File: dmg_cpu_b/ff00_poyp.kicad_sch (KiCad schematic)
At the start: 67 parts, among them P10 IOBUF_B, P11 IOBUF_B, P12 IOBUF_B, P13 IOBUF_B, P14 OBUF_B, P15 OBUF_B

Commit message: First lot of fixes based on issues found.
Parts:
- removed ADYR, AFOP: INVERTER_B, symbol DMG_CPU_Cells:INVERTER_B
- removed AJEC, AKAJ, ANOC, ARAR, ASUZ, ATAJ, BEDA, BENU: TRI_INV_IF0, symbol DMG_CPU_Cells:TRI_INV_IF0
- removed APYS: NOR_2, symbol DMG_CPU_Cells:NOR_2
- removed AXYN: INVERTER_A, symbol DMG_CPU_Cells:INVERTER_A
- ACAT: value NAND_4 -> AND_4; symbol DMG_CPU_Cells:NAND_4 -> DMG_CPU_Cells:AND_4
- CUDY, JEKU, KEMA, KOCE, KURO, KUVE: value TRI_INV_IF1 -> TRI_INV_IF0; symbol DMG_CPU_Cells:TRI_INV_IF1 -> DMG_CPU_Cells:TRI_INV_IF0
- gave numbers to parts that had none: 2
- renumbered JEKU to KOLO
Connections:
- net FF60_D0: now also SIN.3 (~{ENA}_PU)
- net GND: no longer SIN.3 (~{ENA}_PU)
- net at AWOB.2 (D), BATU.3 (D), KERY.5: no longer ASOK.2
- net at ACEF.3 (D), BATU.6 (Q): now also ASOK.2
- net SIN renamed ~{SIN}
- net ~{FF00RD} renamed FF00RD
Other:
- note removed: "This part is in theory never activated."
- moved on the sheet: AKUG, AMUS, ANAP, ATOZ, BYKO

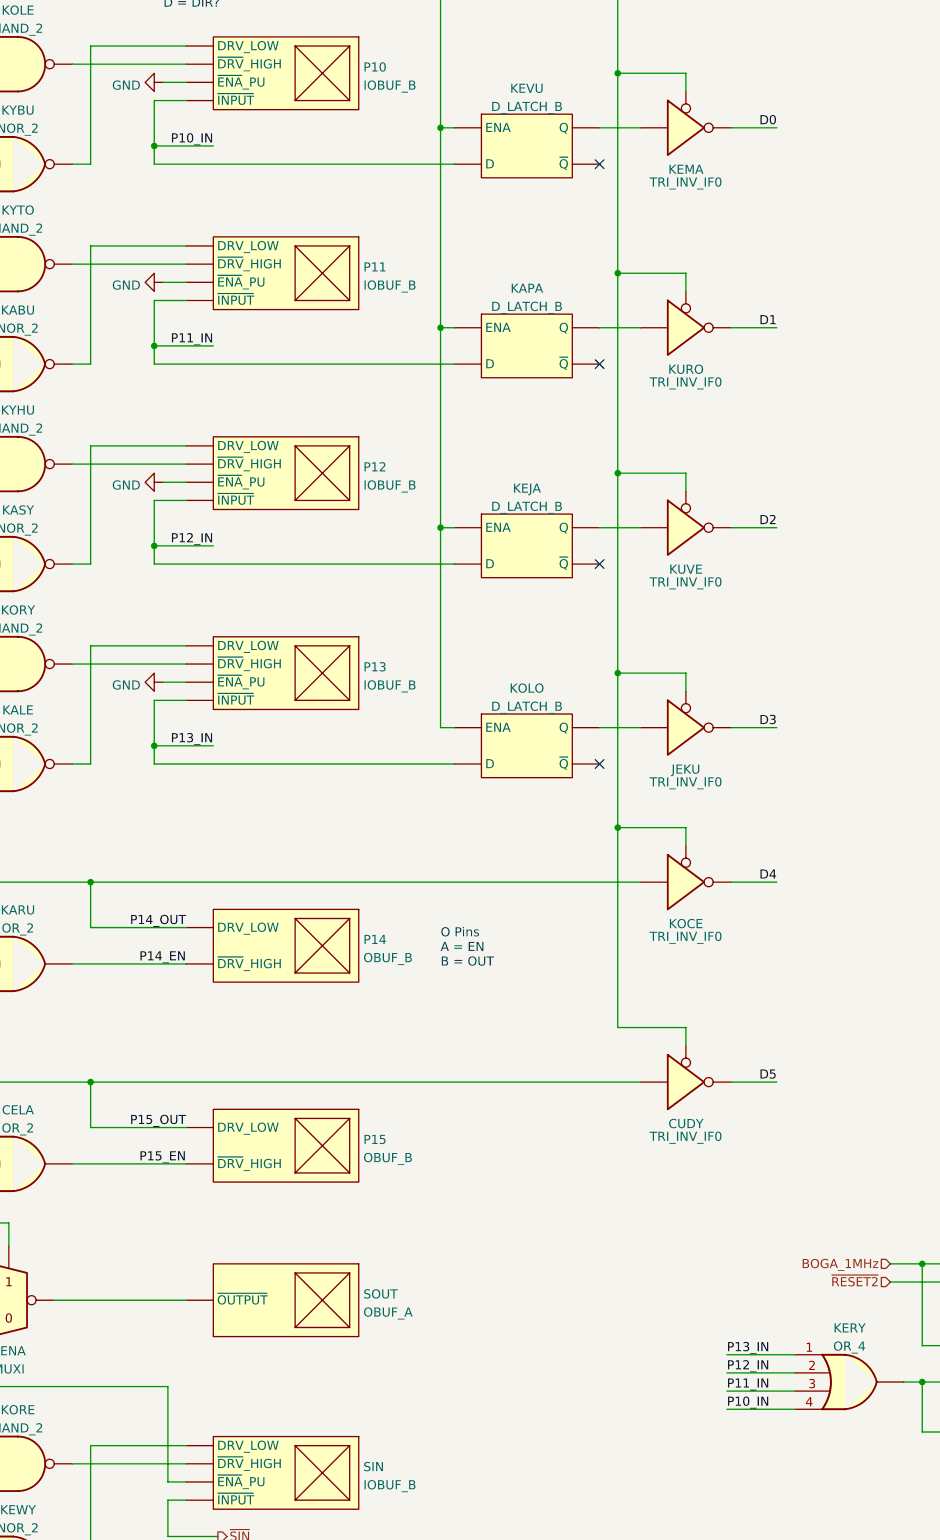
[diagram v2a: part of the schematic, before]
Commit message: CH1 SWEEP page added.
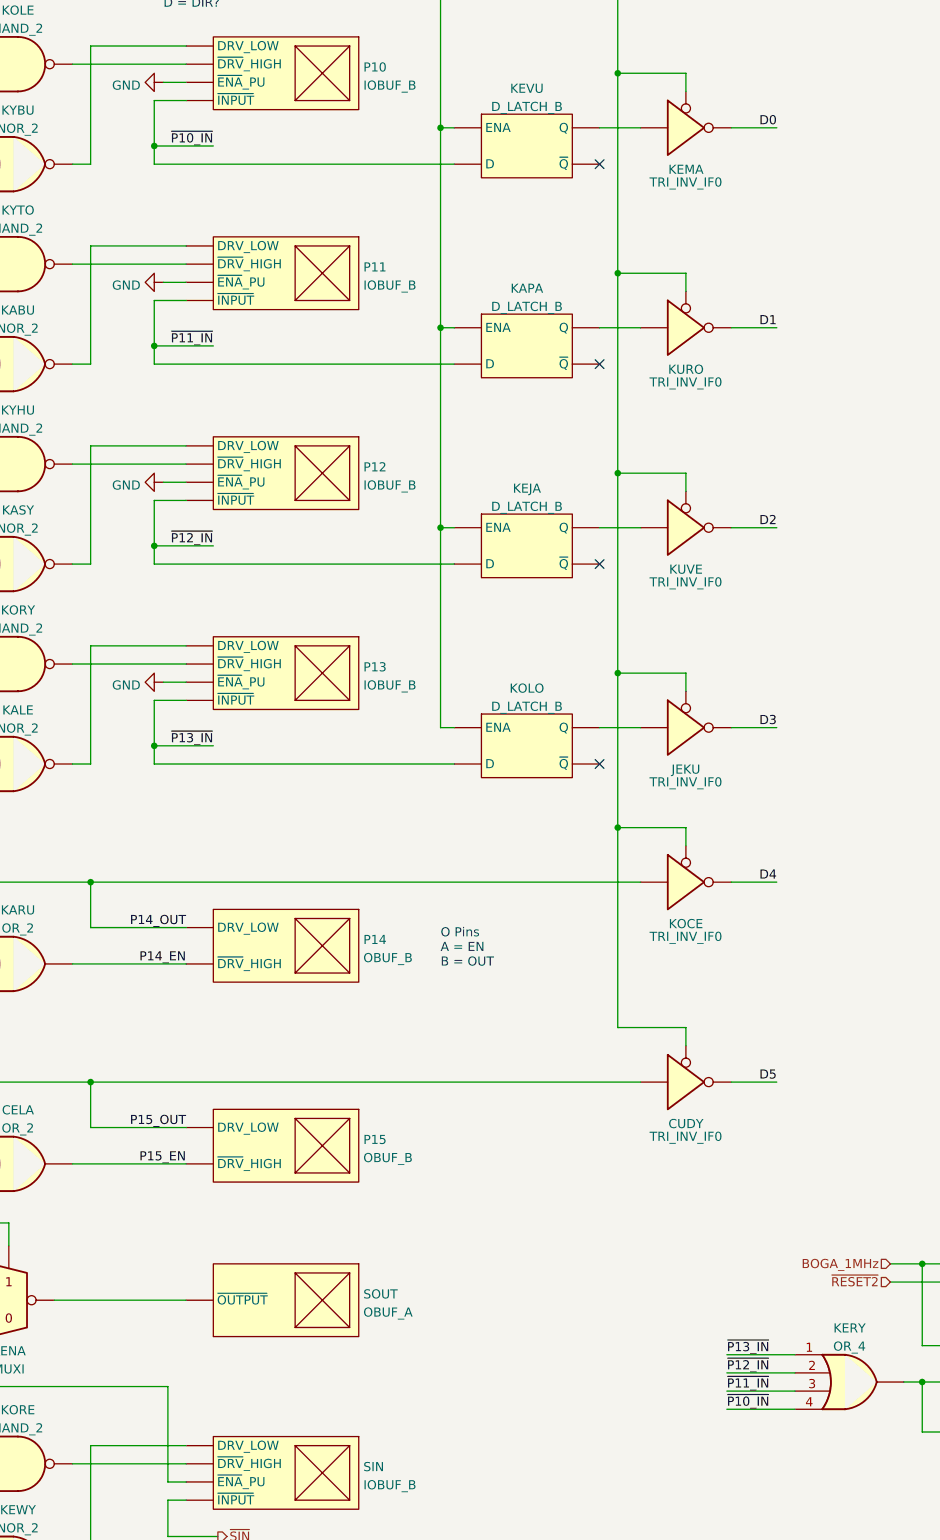
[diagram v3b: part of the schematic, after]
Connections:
- net P10_IN renamed ~{P10_IN}
- net P11_IN renamed ~{P11_IN}
- net P12_IN renamed ~{P12_IN}
- net P13_IN renamed ~{P13_IN}
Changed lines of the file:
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@@
     (effects (font (size 1.27 1.27)) (justify left bottom))
   )
-  (label "P13_IN" (at 184.15 226.695 0)
+  (label "~{P13_IN}" (at 184.15 226.695 0)
     (effects (font (size 1.27 1.27)) (justify left bottom))
   )
-  (label "P11_IN" (at 184.15 231.775 0)
+  (label "~{P11_IN}" (at 184.15 231.775 0)
     (effects (font (size 1.27 1.27)) (justify left bottom))
   )
@@
     (effects (font (size 1.27 1.27)) (justify right bottom))
   )
-  (label "P12_IN" (at 184.15 229.235 0)
+  (label "~{P12_IN}" (at 184.15 229.235 0)
     (effects (font (size 1.27 1.27)) (justify left bottom))
   )
-  (label "P11_IN" (at 112.395 85.725 180)
+  (label "~{P11_IN}" (at 112.395 85.725 180)
     (effects (font (size 1.27 1.27)) (justify right bottom))
   )
@@
     (effects (font (size 1.27 1.27)) (justify right bottom))
   )
-  (label "P13_IN" (at 112.395 141.605 180)
+  (label "~{P13_IN}" (at 112.395 141.605 180)
     (effects (font (size 1.27 1.27)) (justify right bottom))
   )
@@
     (effects (font (size 1.27 1.27)) (justify left bottom))
   )
-  (label "P10_IN" (at 184.15 234.315 0)
+  (label "~{P10_IN}" (at 184.15 234.315 0)
     (effects (font (size 1.27 1.27)) (justify left bottom))
   )
@@
     (effects (font (size 1.27 1.27)) (justify right bottom))
   )
-  (label "P10_IN" (at 112.395 57.785 180)
+  (label "~{P10_IN}" (at 112.395 57.785 180)
     (effects (font (size 1.27 1.27)) (justify right bottom))
   )
@@
     (effects (font (size 1.27 1.27)) (justify left bottom))
   )
-  (label "P12_IN" (at 112.395 113.665 180)
+  (label "~{P12_IN}" (at 112.395 113.665 180)
     (effects (font (size 1.27 1.27)) (justify right bottom))
   )

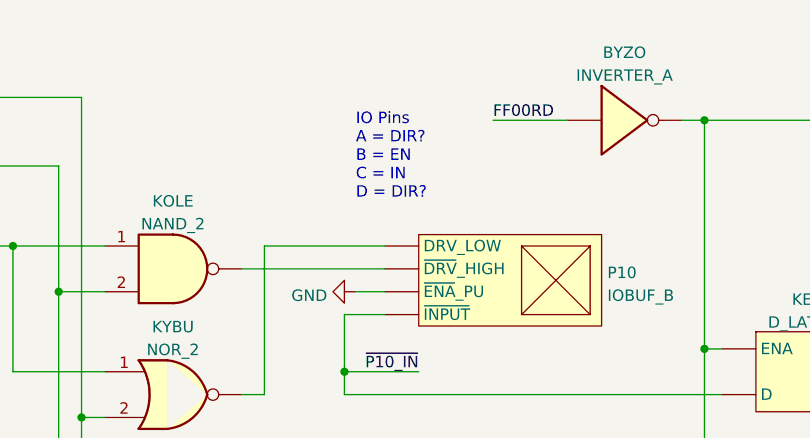
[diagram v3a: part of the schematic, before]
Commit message: fixes made following review
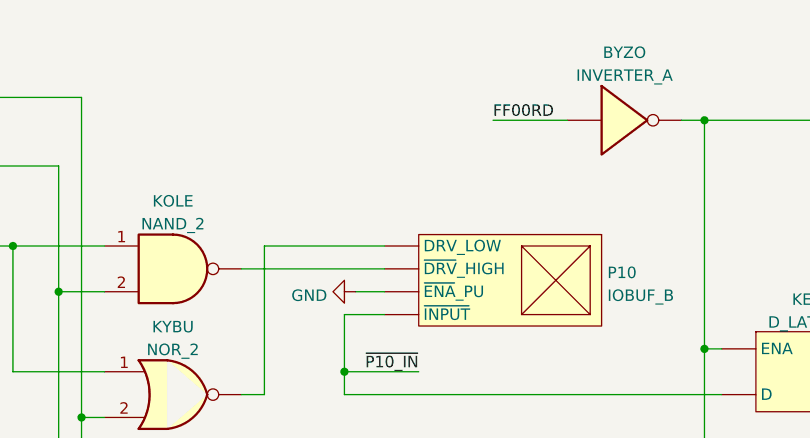
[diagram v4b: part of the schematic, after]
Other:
- note removed: "IO Pins A = DIR? B = EN C = IN D = DIR?"
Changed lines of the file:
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@@
-    (effects (font (size 1.27 1.27)) (justify left bottom))
-  )
-  (text "IO Pins\nA = DIR?\nB = EN\nC = IN\nD = DIR?" (at 105.41 38.735 0)
     (effects (font (size 1.27 1.27)) (justify left bottom))
   )

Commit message: VRAM interface sheet added but various edits in existing sheets. Notable merge of RESET, CLOCKS and FF04 DIV sheets
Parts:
- added AMUT, BURO: DFFR_B2, symbol DMG_CPU_Cells:DFFR_B2
- added APER: NAND_5, symbol DMG_CPU_Cells:NAND_5
- added APET: OR_2, symbol DMG_CPU_Cells:OR_2
- renumbered KEWY to KYWE
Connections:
- net A5: now also APER.2
- net A6: now also APER.3
- net CPU_WR: now also APER.4
- net D0: now also BURO.3 (D)
- net D1: now also AMUT.3 (D)
- net FF60_D0: now also BURO.6 (Q)
- net ~{RESET2}: now also AMUT.2 (~{RESET}), AMUT.4 (~{RESET}), BURO.2 (~{RESET}), BURO.4 (~{RESET})
- net ANAP renamed FF00_FF20_FF40_FF60
- net FF00_FF20_FF40_FF60: now also APER.5
- net TO_CPU2 renamed CPU_WAKEUP
- new net: APER.1, APET.3
- new net FF60WR: AMUT.1 (CLK), APER.6, BURO.1 (CLK)
- new net FF60_D1: AMUT.6 (Q)
- new net T1~{T2}: APET.2
- new net ~{T1}T2: APET.1
- no-connect marks 17 -> 19
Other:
- note added: "FF00 JP"
- note added: "FF60"
- note added: "FF60 - Only writable when in test mode T1 xor T2"
- moved on the sheet: ACAT, ACEF, AGEM, AKUG, APUG, ASOK, ATOZ, AWOB, BATU, BYKO, BYZO, CELA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

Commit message: Minor tweaks to help with clarity.
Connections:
- net T1~{T2}: now also APET.1; no longer APET.2
- net ~{T1}T2: now also APET.2; no longer APET.1
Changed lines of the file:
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@@
     (effects (font (size 1.27 1.27)) (justify left))
   )
-  (hierarchical_label "~{T1}T2" (shape input) (at 87.63 234.315 180)
+  (hierarchical_label "T1~{T2}" (shape input) (at 87.63 234.315 180)
     (effects (font (size 1.27 1.27)) (justify right))
   )
-  (hierarchical_label "T1~{T2}" (shape input) (at 87.63 239.395 180)
+  (hierarchical_label "~{T1}T2" (shape input) (at 87.63 239.395 180)
     (effects (font (size 1.27 1.27)) (justify right))
   )
